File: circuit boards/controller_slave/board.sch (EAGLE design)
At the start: 60 parts, among them IC1 74HC595N, IC2 74HC595N, IC3 74HC595N, IC4 7805TV, Q1 14,7456, U1 ATTINY85-20P, X1 MKDSN1,5/2-5,08, X2 MKDSN1,5/2-5,08, X3 MKDSN1,5/2-5,08

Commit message: changed PCB: mostly SMD parts
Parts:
- removed U1: ATTINY85-20P, attiny25_45_85:ATTINY85-20P
- added C6: 100n, rcl:C-EUC0805K
- added JP4: (no value), pinhead:PINHD-1X3
- added R42: 1K, resistor:R-EU_M0805
- added R43: 10K, resistor:R-EU_M0805
- added S1: (no value), switch-omron:10-XX
- added U$1: ATTINY406, My_AVRs:ATTINY406
- C1, C2, C3, C4, C5: device capacitor-wima:C5/3 -> rcl:C-EUC0805K
- C7, C8: value 22pF -> 12pF; device resistor:C-EU025-025X050 -> rcl:C-EUC0805K
- IC1, IC2, IC3: value 74HC595N -> 74HC595D; device 74xx-eu:74HC595N -> 74xx-eu:74HC595D
- Q1: device crystal:CRYSTALHC49S -> crystal:CRYSTALSM49
- R1, R10, R11, R12, R13, R14, R15, R16, R17, R18, R19, R2, R20, R21, R22, R23, R24, R25, R26, R27, R28, R29, R3, R30, R31, R32, R33, R34, R35, R36, R37, R38, R39, R4, R5, R6, R7, R8, R9: device resistor:R-EU_0207/10 -> resistor:R-EU_M0805
- R40, R41: value 500 -> 100; device resistor:R-EU_0207/10 -> resistor:R-EU_M0805
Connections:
- new net N$68: R13.1, R26.1, R39.1, U$1.PC0
- new net N$75: C6.1, JP4.2, R43.2, S1.S, S1.S1, U$1.PA0
- new net N$76: C6.2, R42.2, S1.P, S1.P1
- net +5V: now also JP4.1, R43.1, U$1.VDD; no longer R13.1, R26.1, R39.1, U1.VCC
- net GND: now also JP4.3, R42.1, U$1.GND; no longer U1.GND
- net N$67: now also U$1.PC1; no longer U1.PB1
- net N$69: now also U$1.PB3; no longer U1.PB0
- net N$70: now also U$1.PB2; no longer U1.PB2
- net N$73: now also U$1.PC2; no longer U1.NRES/PB5
- net N$74: now also U$1.PA3; no longer U1.PB4
- net N$78: now also U$1.PB5; no longer U1.PB3
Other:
- note added: "Common-ground for the LEDs"
- note added: "External Crystal: Stabilize the working frequency of the AVR to be able to use the internal UART interface"
- note added: "Power Supply: - 8V Input, 5V output - capacitors for stability"
- note added: "Shift Registers: - driving the LEDs - between every LED and the shift register a resistor is placed - the shift registers are driven by the AVR"
- note added: "UART breakout connected to screw terminal"
- note added: "programming breakout"
- note added: "reset circuit"
- moved on the sheet: C1, C2, C3, C4, C5, C7, C8, IC1, IC1P, IC2, IC2P, IC3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

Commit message: Controller Slave: Lastkapazität Quarz und UPDI Schnittstelle angepasst
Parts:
- C6: value 100n -> 4,7nF
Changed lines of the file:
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@@
 <grid distance="0.1" unitdist="inch" unit="inch" style="lines" multiple="1" display="no" altdistance="0.01" altunitdist="inch" altunit="inch"/>
 <layers>
-<layer number="1" name="Top" color="4" fill="1" visible="yes" active="no"/>
-<layer number="2" name="Route2" color="16" fill="1" visible="yes" active="no"/>
-<layer number="3" name="Route3" color="17" fill="1" visible="yes" active="no"/>
-<layer number="4" name="Route4" color="18" fill="1" visible="yes" active="no"/>
-<layer number="5" name="Route5" color="19" fill="1" visible="yes" active="no"/>
-<layer number="6" name="Route6" color="25" fill="1" visible="yes" active="no"/>
-<layer number="7" name="Route7" color="26" fill="1" visible="yes" active="no"/>
-<layer number="8" name="Route8" color="27" fill="1" visible="yes" active="no"/>
-<layer number="9" name="Route9" color="28" fill="1" visible="yes" active="no"/>
-<layer number="10" name="Route10" color="29" fill="1" visible="yes" active="no"/>
-<layer number="11" name="Route11" color="30" fill="1" visible="yes" active="no"/>
-<layer number="12" name="Route12" color="20" fill="1" visible="yes" active="no"/>
-<layer number="13" name="Route13" color="21" fill="1" visible="yes" active="no"/>
-<layer number="14" name="Route14" color="22" fill="1" visible="yes" active="no"/>
-<layer number="15" name="Route15" color="23" fill="1" visible="yes" active="no"/>
-<layer number="16" name="Bottom" color="1" fill="1" visible="yes" active="no"/>
-<layer number="17" name="Pads" color="2" fill="1" visible="yes" active="no"/>
-<layer number="18" name="Vias" color="2" fill="1" visible="yes" active="no"/>
-<layer number="19" name="Unrouted" color="6" fill="1" visible="yes" active="no"/>
-<layer number="20" name="Dimension" color="24" fill="1" visible="yes" active="no"/>
-<layer number="21" name="tPlace" color="7" fill="1" visible="yes" active="no"/>
-<layer number="22" name="bPlace" color="7" fill="1" visible="yes" active="no"/>
-<layer number="23" name="tOrigins" color="15" fill="1" visible="yes" active="no"/>
-<layer number="24" name="bOrigins" color="15" fill="1" visible="yes" active="no"/>
-<layer number="25" name="tNames" color="7" fill="1" visible="yes" active="no"/>
-<layer number="26" name="bNames" color="7" fill="1" visible="yes" active="no"/>
-<layer number="27" name="tValues" color="7" fill="1" visible="yes" active="no"/>
-<layer number="28" name="bValues" color="7" fill="1" visible="yes" active="no"/>
+<layer number="1" name="Top" color="4" fill="1" visible="no" active="no"/>
+<layer number="2" name="Route2" color="16" fill="1" visible="no" active="no"/>
+<layer number="3" name="Route3" color="17" fill="1" visible="no" active="no"/>
+<layer number="4" name="Route4" color="18" fill="1" visible="no" active="no"/>
+<layer number="5" name="Route5" color="19" fill="1" visible="no" active="no"/>
+<layer number="6" name="Route6" color="25" fill="1" visible="no" active="no"/>
+<layer number="7" name="Route7" color="26" fill="1" visible="no" active="no"/>
+<layer number="8" name="Route8" color="27" fill="1" visible="no" active="no"/>
+<layer number="9" name="Route9" color="28" fill="1" visible="no" active="no"/>
+<layer number="10" name="Route10" color="29" fill="1" visible="no" active="no"/>
+<layer number="11" name="Route11" color="30" fill="1" visible="no" active="no"/>
+<layer number="12" name="Route12" color="20" fill="1" visible="no" active="no"/>
+<layer number="13" name="Route13" color="21" fill="1" visible="no" active="no"/>
+<layer number="14" name="Route14" color="22" fill="1" visible="no" active="no"/>
+<layer number="15" name="Route15" color="23" fill="1" visible="no" active="no"/>
+<layer number="16" name="Bottom" color="1" fill="1" visible="no" active="no"/>
+<layer number="17" name="Pads" color="2" fill="1" visible="no" active="no"/>
+<layer number="18" name="Vias" color="2" fill="1" visible="no" active="no"/>
+<layer number="19" name="Unrouted" color="6" fill="1" visible="no" active="no"/>
+<layer number="20" name="Dimension" color="24" fill="1" visible="no" active="no"/>
+<layer number="21" name="tPlace" color="7" fill="1" visible="no" active="no"/>
+<layer number="22" name="bPlace" color="7" fill="1" visible="no" active="no"/>
+<layer number="23" name="tOrigins" color="15" fill="1" visible="no" active="no"/>
+<layer number="24" name="bOrigins" color="15" fill="1" visible="no" active="no"/>
+<layer number="25" name="tNames" color="7" fill="1" visible="no" active="no"/>
+<layer number="26" name="bNames" color="7" fill="1" visible="no" active="no"/>
+<layer number="27" name="tValues" color="7" fill="1" visible="no" active="no"/>
+<layer number="28" name="bValues" color="7" fill="1" visible="no" active="no"/>
 <layer number="29" name="tStop" color="7" fill="3" visible="no" active="no"/>
 <layer number="30" name="bStop" color="7" fill="6" visible="no" active="no"/>
@@
 <layer number="35" name="tGlue" color="7" fill="4" visible="no" active="no"/>
 <layer number="36" name="bGlue" color="7" fill="5" visible="no" active="no"/>
-<layer number="37" name="tTest" color="7" fill="1" visible="yes" active="no"/>
-<layer number="38" name="bTest" color="7" fill="1" visible="yes" active="no"/>
+<layer number="37" name="tTest" color="7" fill="1" visible="no" active="no"/>
+<layer number="38" name="bTest" color="7" fill="1" visible="no" active="no"/>
 <layer number="39" name="tKeepout" color="4" fill="11" visible="no" active="no"/>
 <layer number="40" name="bKeepout" color="1" fill="11" visible="no" active="no"/>
@@
 <layer number="44" name="Drills" color="7" fill="1" visible="no" active="no"/>
 <layer number="45" name="Holes" color="7" fill="1" visible="no" active="no"/>
-<layer number="46" name="Milling" color="3" fill="1" visible="yes" active="no"/>
-<layer number="47" name="Measures" color="7" fill="1" visible="yes" active="no"/>
-<layer number="48" name="Document" color="7" fill="1" visible="yes" active="no"/>
-<layer number="49" name="Reference" color="7" fill="1" visible="yes" active="no"/>
-<layer number="51" name="tDocu" color="7" fill="1" visible="yes" active="no"/>
-<layer number="52" name="bDocu" color="7" fill="1" visible="yes" active="no"/>
+<layer number="46" name="Milling" color="3" fill="1" visible="no" active="no"/>
+<layer number="47" name="Measures" color="7" fill="1" visible="no" active="no"/>
+<layer number="48" name="Document" color="7" fill="1" visible="no" active="no"/>
+<layer number="49" name="Reference" color="7" fill="1" visible="no" active="no"/>
+<layer number="51" name="tDocu" color="7" fill="1" visible="no" active="no"/>
+<layer number="52" name="bDocu" color="7" fill="1" visible="no" active="no"/>
 <layer number="88" name="SimResults" color="9" fill="1" visible="yes" active="yes"/>
 <layer number="89" name="SimProbes" color="9" fill="1" visible="yes" active="yes"/>
@@
 <part name="GND11" library="supply1" library_urn="urn:adsk.eagle:library:371" deviceset="GND" device=""/>
 <part name="P+9" library="supply1" library_urn="urn:adsk.eagle:library:371" deviceset="+5V" device=""/>
-<part name="C6" library="rcl" library_urn="urn:adsk.eagle:library:334" deviceset="C-EU" device="C0805K" package3d_urn="urn:adsk.eagle:package:23681/2" value="100n"/>
+<part name="C6" library="rcl" library_urn="urn:adsk.eagle:library:334" deviceset="C-EU" device="C0805K" package3d_urn="urn:adsk.eagle:package:23681/2" value="4,7nF"/>
 <part name="R42" library="resistor" library_urn="urn:adsk.eagle:library:348" deviceset="R-EU_" device="M0805" value="1K"/>
 <part name="R43" library="resistor" library_urn="urn:adsk.eagle:library:348" deviceset="R-EU_" device="M0805" value="10K"/>

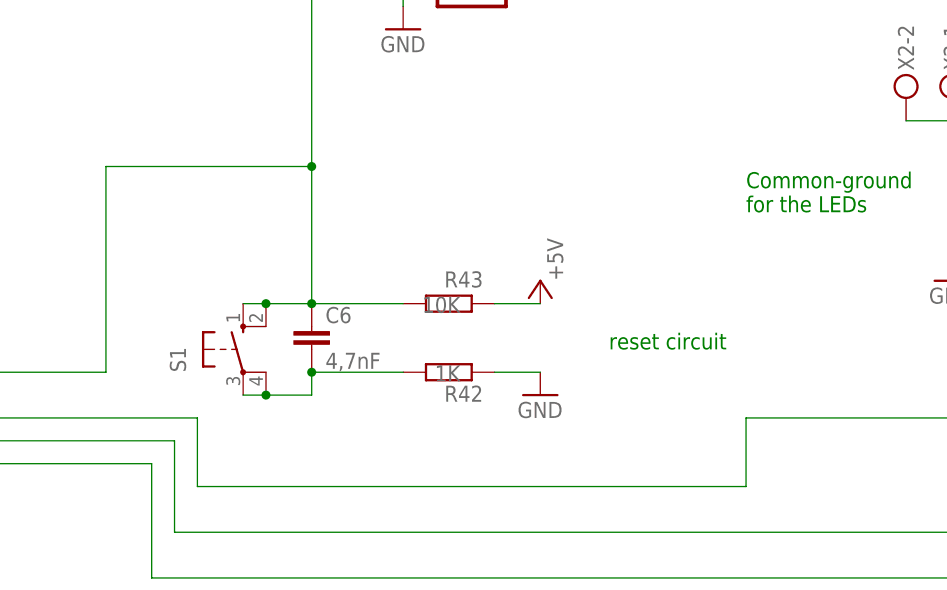
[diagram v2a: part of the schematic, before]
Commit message: removed reset circuit from board design
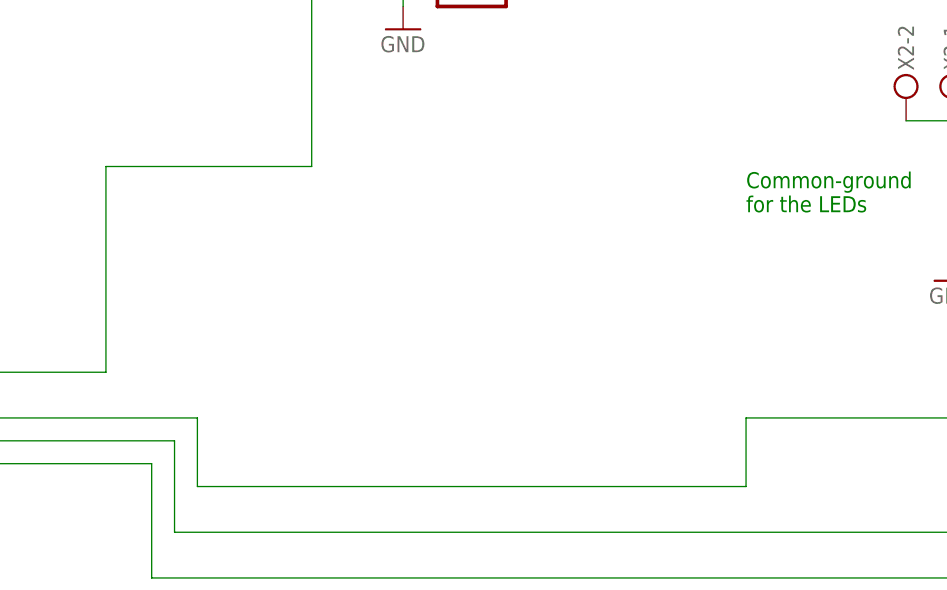
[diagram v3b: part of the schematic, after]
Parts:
- removed C6: 4,7nF, rcl:C-EUC0805K
- removed R42: 1K, resistor:R-EU_M0805
- removed R43: 10K, resistor:R-EU_M0805
- removed S1: (no value), switch-omron:10-XX
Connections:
- removed net N$76: C6.2, R42.2, S1.P, S1.P1
- net +5V: no longer R43.1
- net GND: no longer R42.1
- net N$75: no longer C6.1, R43.2, S1.S, S1.S1
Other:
- note removed: "reset circuit"
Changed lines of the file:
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@@
 <part name="GND11" library="supply1" library_urn="urn:adsk.eagle:library:371" deviceset="GND" device=""/>
 <part name="P+9" library="supply1" library_urn="urn:adsk.eagle:library:371" deviceset="+5V" device=""/>
-<part name="C6" library="rcl" library_urn="urn:adsk.eagle:library:334" deviceset="C-EU" device="C0805K" package3d_urn="urn:adsk.eagle:package:23681/2" value="4,7nF"/>
-<part name="R42" library="resistor" library_urn="urn:adsk.eagle:library:348" deviceset="R-EU_" device="M0805" value="1K"/>
-<part name="R43" library="resistor" library_urn="urn:adsk.eagle:library:348" deviceset="R-EU_" device="M0805" value="10K"/>
-<part name="S1" library="switch-omron" library_urn="urn:adsk.eagle:library:377" deviceset="10-XX" device="" package3d_urn="urn:adsk.eagle:package:27496/1"/>
-<part name="P+10" library="supply1" library_urn="urn:adsk.eagle:library:371" deviceset="+5V" device=""/>
-<part name="GND12" library="supply1" library_urn="urn:adsk.eagle:library:371" deviceset="GND" device=""/>
 </parts>
 <sheets>
@@
 <text x="254" y="93.98" size="1.778" layer="91">Common-ground
 for the LEDs</text>
-<text x="238.76" y="78.74" size="1.778" layer="91">reset circuit</text>
 <text x="231.14" y="121.92" size="1.778" layer="91">programming breakout</text>
 </plain>
@@
 <instance part="P+9" gate="1" x="215.9" y="129.54" smashed="yes">
 <attribute name="VALUE" x="213.36" y="124.46" size="1.778" layer="96" rot="R90"/>
-</instance>
-<instance part="C6" gate="G$1" x="205.74" y="81.28" smashed="yes">
-<attribute name="NAME" x="207.264" y="81.661" size="1.778" layer="95"/>
-<attribute name="VALUE" x="207.264" y="76.581" size="1.778" layer="96"/>
-</instance>
-<instance part="R42" gate="G$1" x="220.98" y="76.2" smashed="yes" rot="R180">
-<attribute name="NAME" x="224.79" y="74.7014" size="1.778" layer="95" rot="R180"/>
-<attribute name="VALUE" x="222.25" y="76.962" size="1.778" layer="96" rot="R180"/>
-</instance>
-<instance part="R43" gate="G$1" x="220.98" y="83.82" smashed="yes" rot="R180">
-<attribute name="NAME" x="224.79" y="87.4014" size="1.778" layer="95" rot="R180"/>
-<attribute name="VALUE" x="222.25" y="84.582" size="1.778" layer="96" rot="R180"/>
-</instance>
-<instance part="S1" gate="1" x="198.12" y="78.74" smashed="yes">
-<attribute name="NAME" x="191.77" y="76.2" size="1.778" layer="95" rot="R90"/>
-<attribute name="VALUE" x="194.31" y="81.915" size="1.778" layer="96" rot="R90"/>
-</instance>
-<instance part="P+10" gate="1" x="231.14" y="86.36" smashed="yes">
-<attribute name="VALUE" x="233.68" y="86.36" size="1.778" layer="96" rot="R90"/>
-</instance>
-<instance part="GND12" gate="1" x="231.14" y="73.66" smashed="yes">
-<attribute name="VALUE" x="228.6" y="71.12" size="1.778" layer="96"/>
 </instance>
 </instances>
@@
 <wire x1="215.9" y1="119.38" x2="215.9" y2="116.84" width="0.1524" layer="91"/>
 </segment>
-<segment>
-<pinref part="GND12" gate="1" pin="GND"/>
-<pinref part="R42" gate="G$1" pin="1"/>
-<wire x1="231.14" y1="76.2" x2="226.06" y2="76.2" width="0.1524" layer="91"/>
-</segment>
 </net>
 <net name="+5V" class="0">
@@
 <wire x1="215.9" y1="127" x2="215.9" y2="124.46" width="0.1524" layer="91"/>
 <wire x1="215.9" y1="124.46" x2="223.52" y2="124.46" width="0.1524" layer="91"/>
-</segment>
-<segment>
-<pinref part="R43" gate="G$1" pin="1"/>
-<pinref part="P+10" gate="1" pin="+5V"/>
-<wire x1="226.06" y1="83.82" x2="231.14" y2="83.82" width="0.1524" layer="91"/>
 </segment>
 </net>
@@
 <net name="N$75" class="0">
 <segment>
-<pinref part="S1" gate="1" pin="S"/>
-<pinref part="R43" gate="G$1" pin="2"/>
-<wire x1="198.12" y1="83.82" x2="200.66" y2="83.82" width="0.1524" layer="91"/>
-<pinref part="C6" gate="G$1" pin="1"/>
-<junction x="205.74" y="83.82"/>
-<wire x1="200.66" y1="83.82" x2="205.74" y2="83.82" width="0.1524" layer="91"/>
-<wire x1="205.74" y1="83.82" x2="215.9" y2="83.82" width="0.1524" layer="91"/>
-<pinref part="S1" gate="1" pin="S1"/>
-<junction x="200.66" y="83.82"/>
 <pinref part="JP4" gate="A" pin="2"/>
 <wire x1="223.52" y1="121.92" x2="205.74" y2="121.92" width="0.1524" layer="91"/>
 <wire x1="205.74" y1="121.92" x2="205.74" y2="99.06" width="0.1524" layer="91"/>
 <pinref part="U$1" gate="G$1" pin="PA0"/>
-<wire x1="205.74" y1="99.06" x2="205.74" y2="83.82" width="0.1524" layer="91"/>
 <wire x1="142.24" y1="76.2" x2="182.88" y2="76.2" width="0.1524" layer="91"/>
 <wire x1="182.88" y1="76.2" x2="182.88" y2="99.06" width="0.1524" layer="91"/>
 <wire x1="182.88" y1="99.06" x2="205.74" y2="99.06" width="0.1524" layer="91"/>
-<junction x="205.74" y="99.06"/>
-</segment>
-</net>
-<net name="N$76" class="0">
-<segment>
-<pinref part="R42" gate="G$1" pin="2"/>
-<pinref part="C6" gate="G$1" pin="2"/>
-<wire x1="215.9" y1="76.2" x2="205.74" y2="76.2" width="0.1524" layer="91"/>
-<pinref part="S1" gate="1" pin="P"/>
-<wire x1="198.12" y1="73.66" x2="200.66" y2="73.66" width="0.1524" layer="91"/>
-<wire x1="200.66" y1="73.66" x2="205.74" y2="73.66" width="0.1524" layer="91"/>
-<wire x1="205.74" y1="73.66" x2="205.74" y2="76.2" width="0.1524" layer="91"/>
-<pinref part="S1" gate="1" pin="P1"/>
-<junction x="200.66" y="73.66"/>
-<junction x="205.74" y="76.2"/>
-</segment>
-</net>
+</segment>
+</net>
